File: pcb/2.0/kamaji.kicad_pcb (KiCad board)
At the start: 2 copper layers, 100 x 100 mm, 0 parts

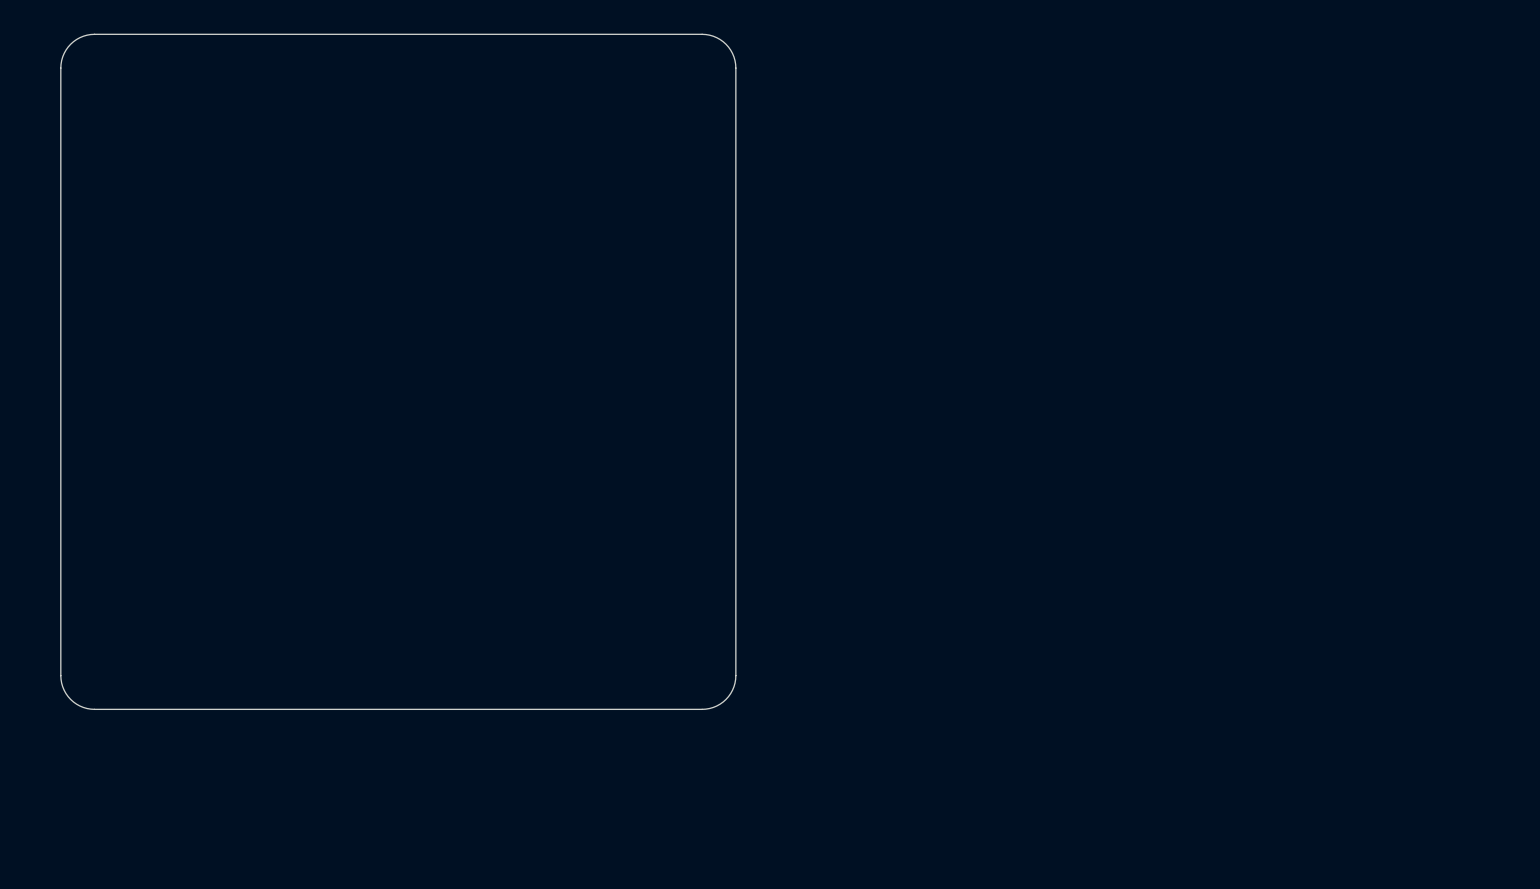
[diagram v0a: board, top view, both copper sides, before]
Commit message: test point, 6th player socket
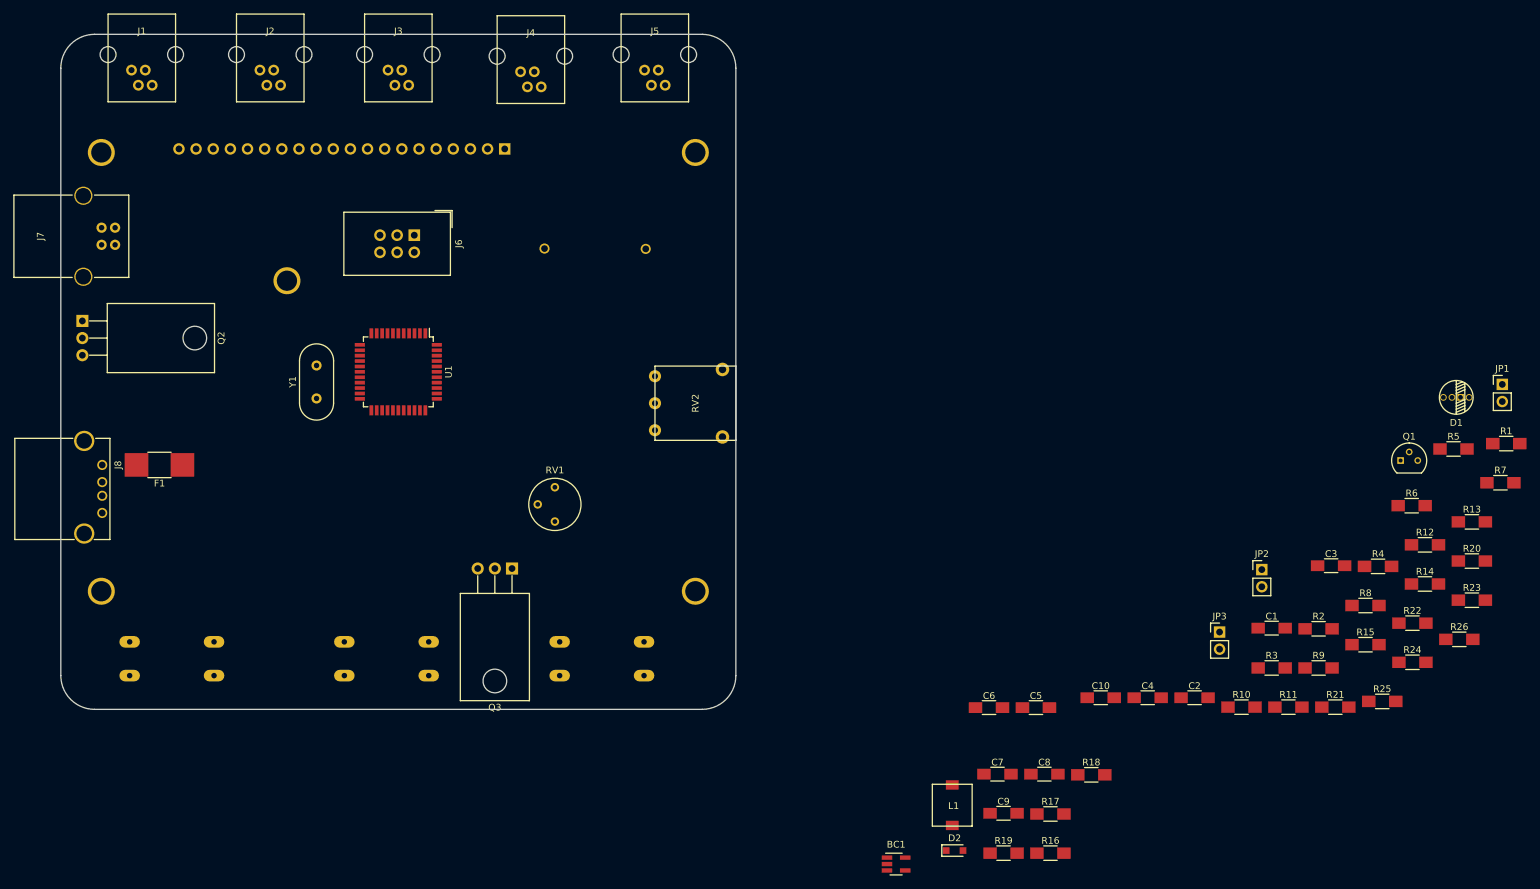
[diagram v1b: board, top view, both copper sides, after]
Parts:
- added BC1: LM27313, TO_SOT_Packages_SMD:SOT-23-5_HandSoldering, F.Cu at (173.7, 172.9)
- added C1: 0.1uF, Capacitors_SMD:C_1206_HandSoldering, F.Cu at (229.4, 138.0)
- added C10: 0.1uF, Capacitors_SMD:C_1206_HandSoldering, F.Cu at (204.1, 148.3)
- added C2: 18pF, Capacitors_SMD:C_1206_HandSoldering, F.Cu at (218.0, 148.3)
- added C3: 18pF, Capacitors_SMD:C_1206_HandSoldering, F.Cu at (238.2, 128.7)
- added C4: 0.1uF, Capacitors_SMD:C_1206_HandSoldering, F.Cu at (211.0, 148.3)
- added C5: 0.1uF, Capacitors_SMD:C_1206_HandSoldering, F.Cu at (194.5, 149.7)
- added C6: 0.1uF, Capacitors_SMD:C_1206_HandSoldering, F.Cu at (187.5, 149.7)
- added C7: 4.7uF, Capacitors_SMD:C_1206_HandSoldering, F.Cu at (188.8, 159.6)
- added C8: 2.2uF, Capacitors_SMD:C_1206_HandSoldering, F.Cu at (195.7, 159.6)
- added C9: 220pF, Capacitors_SMD:C_1206_HandSoldering, F.Cu at (189.7, 165.4)
- added D1: LED_CRGB, kamaji:LED_RGB_common_cathode_5mm, F.Cu at (256.7, 103.8)
- added D2: MBR0540, Diodes_SMD:D_SOD-323_HandSoldering, F.Cu at (182.4, 170.9)
- added DS1: LCD12864B, kamaji:LCD12864, B.Cu at (100.0, 100.0)
- added F1: 1A, Resistors_SMD:R_1812_HandSoldering, F.Cu at (64.6, 113.8)
- added J1: RJ10, kamaji:RJ10, F.Cu at (62.0, 47.0)
- added J2: RJ10, kamaji:RJ10, F.Cu at (81.0, 47.0)
- added J3: RJ10, kamaji:RJ10, F.Cu at (100.0, 47.0)
- added J4: RJ10, kamaji:RJ10, F.Cu at (119.6, 47.2)
- added J5: RJ10, kamaji:RJ10, F.Cu at (138.0, 47.0)
- added J6: ICSP, Connectors_IDC:IDC-Header_2x03_Pitch2.54mm_Straight, F.Cu at (102.4, 79.8)
- added J7: USB_B, Connectors:USB_B, F.Cu at (58.0, 81.2)
- added J8: USB_A, Connectors:USB_A, F.Cu at (56.1, 113.8)
- added JP1: Jumper, Socket_Strips:Socket_Strip_Straight_1x02_Pitch2.54mm, F.Cu at (263.5, 101.9)
- added JP2: Jumper_NC_Small, Socket_Strips:Socket_Strip_Straight_1x02_Pitch2.54mm, F.Cu at (227.9, 129.3)
- added JP3: SoundVcc2, Socket_Strips:Socket_Strip_Straight_1x02_Pitch2.54mm, F.Cu at (221.7, 138.5)
- added L1: 10uH, kamaji:Inductor_PIS2408_SMD, F.Cu at (182.1, 164.2)
- added LS1: Speaker_Crystal, kamaji:buzzer_30x17, B.Cu at (129.2, 81.7)
- added Q1: 2N3904, TO_SOT_Packages_THT:TO-92_Molded_Narrow, F.Cu at (248.5, 113.1)
- added Q2: IRL540N, TO_SOT_Packages_THT:TO-220-3_Horizontal, F.Cu at (53.2, 92.5)
- added Q3: IRL540N, TO_SOT_Packages_THT:TO-220-3_Horizontal, F.Cu at (116.8, 129.1)
- added R1: 22R, Resistors_SMD:R_1206_HandSoldering, F.Cu at (264.1, 110.6)
- added R10: 220R, Resistors_SMD:R_1206_HandSoldering, F.Cu at (224.9, 149.7)
- added R11: 220R, Resistors_SMD:R_1206_HandSoldering, F.Cu at (231.9, 149.7)
- added R12: 220R, Resistors_SMD:R_1206_HandSoldering, F.Cu at (252.1, 125.6)
- added R13: 1K, Resistors_SMD:R_1206_HandSoldering, F.Cu at (259.0, 122.2)
- added R14: 0, Resistors_SMD:R_1206_HandSoldering, F.Cu at (252.1, 131.4)
- added R15: 10K, Resistors_SMD:R_1206_HandSoldering, F.Cu at (243.3, 140.4)
- added R16: 51K, Resistors_SMD:R_1206_HandSoldering, F.Cu at (196.6, 171.3)
- added R17: 31K3, Resistors_SMD:R_1206_HandSoldering, F.Cu at (196.6, 165.5)
- added R18: 100K, Resistors_SMD:R_1206_HandSoldering, F.Cu at (202.7, 159.7)
- added R19: 0, Resistors_SMD:R_1206_HandSoldering, F.Cu at (189.7, 171.3)
- added R2: 22R, Resistors_SMD:R_1206_HandSoldering, F.Cu at (236.3, 138.1)
- added R20: 10K, Resistors_SMD:R_1206_HandSoldering, F.Cu at (259.0, 128.0)
- added R21: 200R, Resistors_SMD:R_1206_HandSoldering, F.Cu at (238.8, 149.7)
- added R22: 200R, Resistors_SMD:R_1206_HandSoldering, F.Cu at (250.2, 137.2)
- added R23: 200R, Resistors_SMD:R_1206_HandSoldering, F.Cu at (259.0, 133.8)
- added R24: 200R, Resistors_SMD:R_1206_HandSoldering, F.Cu at (250.2, 143.0)
- added R25: 10K, Resistors_SMD:R_1206_HandSoldering, F.Cu at (245.8, 148.8)
- added R26: 10K, Resistors_SMD:R_1206_HandSoldering, F.Cu at (257.2, 139.6)
- added R3: 10K, Resistors_SMD:R_1206_HandSoldering, F.Cu at (229.4, 143.9)
- added R4: 220R, Resistors_SMD:R_1206_HandSoldering, F.Cu at (245.1, 128.8)
- added R5: 220R, Resistors_SMD:R_1206_HandSoldering, F.Cu at (256.3, 111.4)
- added R6: 220R, Resistors_SMD:R_1206_HandSoldering, F.Cu at (250.1, 119.8)
- added R7: 220R, Resistors_SMD:R_1206_HandSoldering, F.Cu at (263.3, 116.4)
- added R8: 10K, Resistors_SMD:R_1206_HandSoldering, F.Cu at (243.3, 134.6)
- added R9: 220R, Resistors_SMD:R_1206_HandSoldering, F.Cu at (236.3, 143.9)
- added RV1: 200K, Potentiometers:Potentiometer_Trimmer_Bourns_3339P_Horizontal, F.Cu at (123.2, 122.2)
- added RV2: VOLUME, kamaji:Potentiometer_Wheel_16mm, F.Cu at (144.0, 104.6)
- added SW1: SW_Push, Buttons_Switches_THT:SW_PUSH-12mm, B.Cu at (60.2, 145.0)
- added SW2: SW_Push, Buttons_Switches_THT:SW_PUSH-12mm, B.Cu at (92.0, 145.0)
- added SW3: SW_Push, Buttons_Switches_THT:SW_PUSH-12mm, B.Cu at (123.9, 145.0)
- added U1: ATMEGA32U4-AU, Housings_QFP:TQFP-44_10x10mm_Pitch0.8mm, F.Cu at (100.0, 100.0)
- added Y1: 16MHz, Crystals:Crystal_HC49-U_Vertical, F.Cu at (87.9, 103.9)

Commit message: place the RJ10 sockets on the PCB
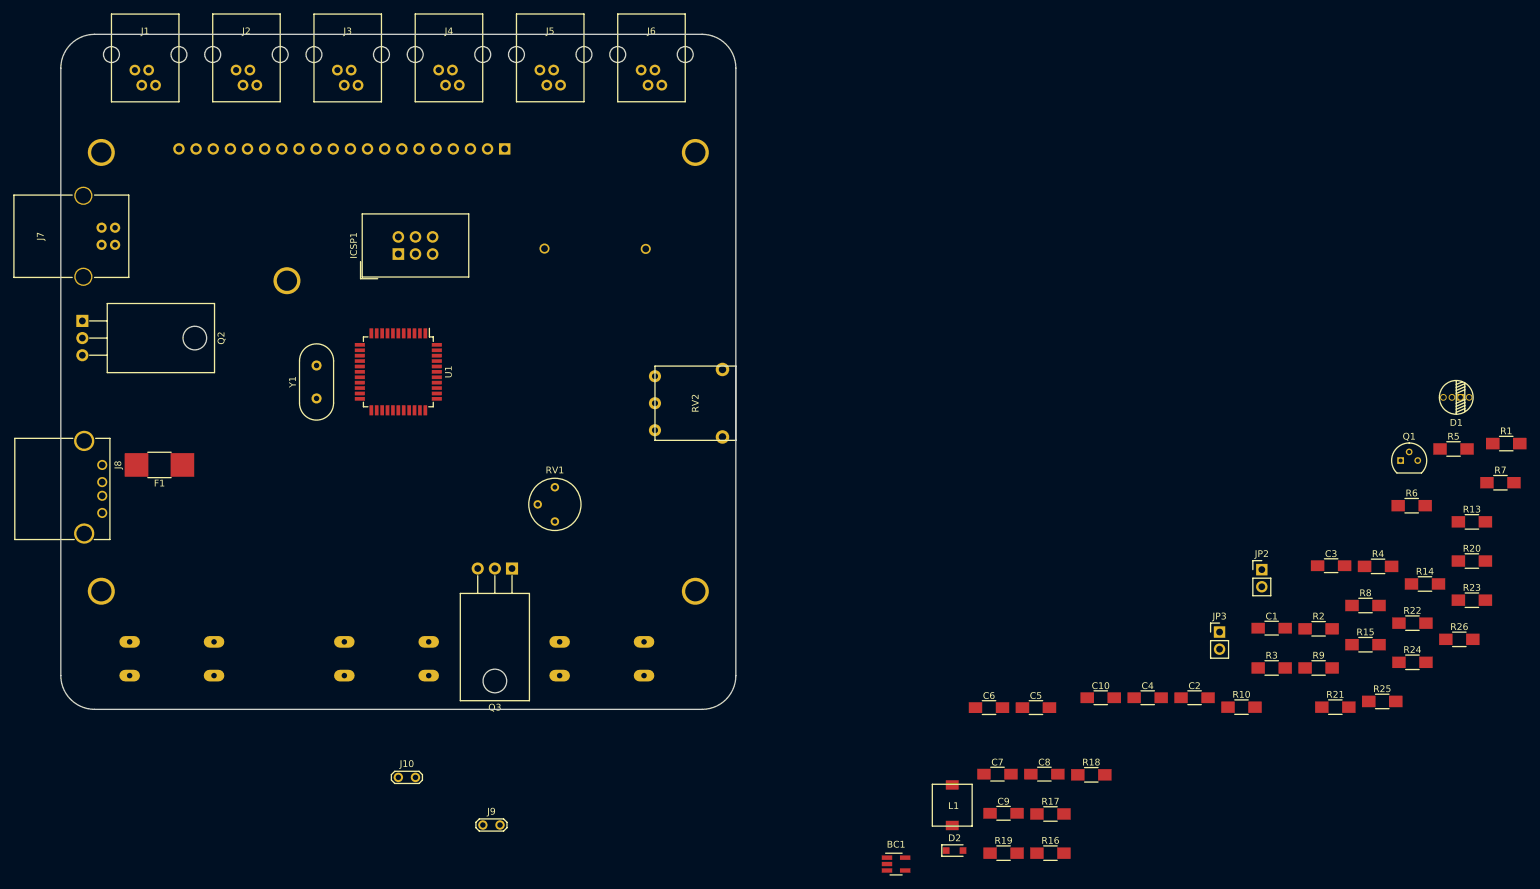
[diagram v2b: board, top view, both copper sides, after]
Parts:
- removed JP1: Jumper, Socket_Strips:Socket_Strip_Straight_1x02_Pitch2.54mm
- removed R11, R12: 220R, Resistors_SMD:R_1206_HandSoldering
- added ICSP1: ICSP, Connectors_IDC:IDC-Header_2x03_Pitch2.54mm_Straight, F.Cu at (100.0, 82.5)
- added J10: TEST_5V, Measurement_Points:Test_Point_2Pads, F.Cu at (100.0, 160.1)
- added J9: TEST_28V, Measurement_Points:Test_Point_2Pads, F.Cu at (112.5, 167.1)
- J6: value ICSP -> RJ10; footprint Connectors_IDC:IDC-Header_2x03_Pitch2.54mm_Straight -> kamaji:RJ10
- moved J6 48.0 mm to (137.5, 47.0), turned to 180 degrees
- moved J5 15.5 mm to (122.5, 47.0)
- moved J4 12.1 mm to (107.5, 47.0)
- moved J3 7.50 mm to (92.5, 47.0)
- moved J2 3.53 mm to (77.5, 47.0)
- moved J1 0.50 mm to (62.5, 47.0)
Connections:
- D1 pad 2: Net-(D1-Pad2) -> /SIGNAL_R
- D1 pad 3: Net-(D1-Pad3) -> /SIGNAL_G
- D1 pad 4: Net-(D1-Pad4) -> /SIGNAL_B
- J6 pad 1: /MISO -> +28V
- J6 pad 2: VCC -> Net-(J6-Pad2)
- J6 pad 3: /SCK -> +28V
- J6 pad 4: /MOSI -> /PBTN6
- J7 pad 1: Net-(J7-Pad1) -> Net-(F1-Pad1)
- R10 pad 1: Net-(D1-Pad4) -> Net-(J6-Pad2)
- R10 pad 2: /SIGNAL_R -> /PLED6
- U1 pad 22: Net-(U1-Pad22) -> /PLED6
- U1 pad 39: Net-(U1-Pad39) -> /PBTN6

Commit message: roughly place components on the PCB
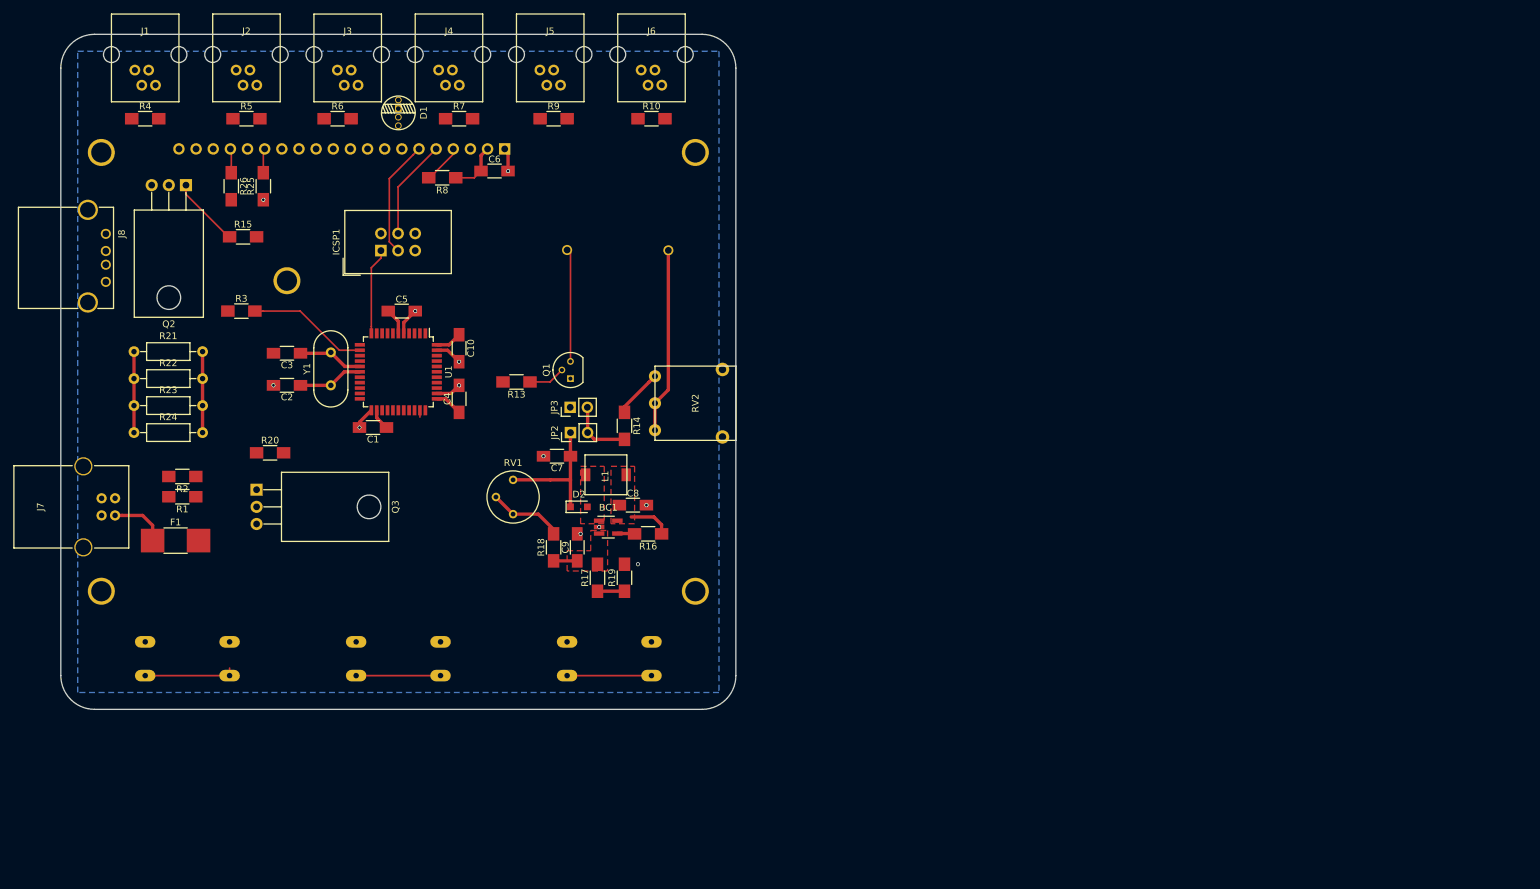
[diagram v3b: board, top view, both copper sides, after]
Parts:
- removed J10: TEST_5V, Measurement_Points:Test_Point_2Pads
- removed J9: TEST_28V, Measurement_Points:Test_Point_2Pads
- R21, R22, R23, R24: footprint Resistors_SMD:R_1206_HandSoldering -> Resistors_THT:R_Axial_DIN0207_L6.3mm_D2.5mm_P10.16mm_Horizontal
- moved R23 200.3 mm to (60.8, 105.0)
- moved R1 196.3 mm to (68.0, 118.5), turned to 180 degrees
- moved R4 194.3 mm to (62.5, 62.5)
- moved R26 193.9 mm to (75.2, 72.5), turned to 270 degrees
- moved R22 192.8 mm to (60.8, 101.0)
- moved R24 192.4 mm to (60.8, 109.0)
- moved R21 185.6 mm to (60.8, 97.0)
- moved R5 185.4 mm to (77.5, 62.5)
- moved R25 182.5 mm to (80.0, 72.5), turned to 90 degrees
- moved R20 178.8 mm to (81.0, 112.0)
- moved R15 176.9 mm to (77.0, 80.0)
- moved R2 169.8 mm to (68.0, 115.5), turned to 180 degrees
- moved R6 169.1 mm to (91.0, 62.5)
- moved R7 163.4 mm to (109.0, 62.5)
- moved D1 162.3 mm to (100.0, 61.6), turned to 90 degrees
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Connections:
- net Net-(BC1-Pad3) renamed /Boost Converter/BOOST_FB
- BC1 pad 2: +28V -> GND
- C1 pad 2: +28V -> GND
- C10 pad 2: +28V -> GND
- C2 pad 2: +28V -> GND
- C3 pad 2: +28V -> GND
- C4 pad 2: +28V -> GND
- C5 pad 2: +28V -> GND
- C6 pad 2: +28V -> GND
- C7 pad 1: +28V -> /Boost Converter/BOOST_VOUT
- C7 pad 2: +28V -> GND
- C8 pad 2: +28V -> GND
- C9 pad 2: +28V -> GND
- D1 pad 1: +28V -> GND
- D2 pad 1: +28V -> /Boost Converter/BOOST_VOUT
- DS1 pad 1: +28V -> GND
- DS1 pad 10: +28V -> GND
- DS1 pad 11: +28V -> GND
- DS1 pad 12: +28V -> GND
- DS1 pad 13: +28V -> GND
- DS1 pad 14: +28V -> GND
- DS1 pad 16: Net-(DS1-Pad16) -> (no net)
- DS1 pad 18: Net-(DS1-Pad18) -> (no net)
- DS1 pad 20: +28V -> GND
- DS1 pad 3: Net-(DS1-Pad3) -> (no net)
- DS1 pad 7: +28V -> GND
- DS1 pad 8: +28V -> GND
- DS1 pad 9: +28V -> GND
- ICSP1 pad 6: +28V -> GND
- J1 pad 1: +28V -> GND
- J1 pad 3: +28V -> GND
- J2 pad 1: +28V -> GND
- J2 pad 3: +28V -> GND
- J3 pad 1: +28V -> GND
- J3 pad 3: +28V -> GND
- J4 pad 1: +28V -> GND
- J4 pad 3: +28V -> GND
- J5 pad 1: +28V -> GND
- J5 pad 3: +28V -> GND
- J6 pad 1: +28V -> GND
- J6 pad 3: +28V -> GND
- J7 pad 4: +28V -> GND
- J7 pad 5: +28V -> GND
- J8 pad 2: Net-(J8-Pad2) -> (no net)
- J8 pad 3: Net-(J8-Pad3) -> (no net)
- J8 pad 5: +28V -> GND
- JP2 pad 1: +28V -> /Boost Converter/BOOST_VOUT
- Q1 pad 1: +28V -> GND
- Q2 pad 3: +28V -> GND
- Q3 pad 3: +28V -> GND
- R15 pad 2: +28V -> GND
- R19 pad 2: +28V -> GND
- R20 pad 2: +28V -> GND
- R25 pad 1: +28V -> GND
- RV1 pad 3: +28V -> /Boost Converter/BOOST_VOUT
- SW1 pad 2: +28V -> GND
- SW2 pad 2: +28V -> GND
- SW3 pad 2: +28V -> GND
- U1 pad 15: +28V -> GND
- U1 pad 23: +28V -> GND
- U1 pad 35: +28V -> GND
- U1 pad 43: +28V -> GND
- U1 pad 5: +28V -> GND
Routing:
- net VCC: track 0.00 -> 37.5 mm
- net Net-(LS1-Pad1): track 0.00 -> 27.5 mm
- net /Boost Converter/BOOST_VOUT: track 0.00 -> 20.5 mm
- net GND: track 0.00 -> 18.6 mm, vias 0 -> 11
- net /RST: track 0.00 -> 18.0 mm
- net /SCK: track 0.00 -> 17.8 mm
- net Net-(LS1-Pad2): track 0.00 -> 17.0 mm
- net /MOSI: track 0.00 -> 14.9 mm
- net /CBTN1: track 0.00 -> 14.6 mm
- net /CBTN2: track 0.00 -> 13.2 mm
- net /MISO: track 0.00 -> 12.8 mm
- net /CBTN3: track 0.00 -> 12.5 mm
- net Net-(Q3-Pad2): track 0.00 -> 12.0 mm
- net Net-(R18-Pad2): track 0.00 -> 11.4 mm
- net /LAMP: track 0.00 -> 10.4 mm
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- added copper zone on F.Cu, net /Boost Converter/BOOST_FB
- added copper zone on B.Cu, net GND
- added copper zone on F.Cu, net Net-(BC1-Pad1)
- added copper zone on F.Cu, net VCC
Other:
- net class Power added: clearance 0.25, trace_width 0.5, via_dia 0.6, via_drill 0.4
